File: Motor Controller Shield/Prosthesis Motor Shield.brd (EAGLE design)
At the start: 101.6 x 53.3 mm, 51 parts, among them M1_ACT M02POLAR_LOCK, M2_ACT M02POLAR_LOCK, U1 74VHC14MTCX, U2 74VHC14MTCX

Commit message: Routed BMS interface board and added branding.
Changed branding for CCB and MCBs
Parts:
- moved U$1 34.6 mm to (22.5, 11.7)
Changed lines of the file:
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@@
 <layer number="23" name="tOrigins" color="15" fill="1" visible="yes" active="yes"/>
 <layer number="24" name="bOrigins" color="15" fill="1" visible="yes" active="yes"/>
-<layer number="25" name="tNames" color="16" fill="1" visible="no" active="yes"/>
+<layer number="25" name="tNames" color="16" fill="1" visible="yes" active="yes"/>
 <layer number="26" name="bNames" color="7" fill="1" visible="no" active="yes"/>
 <layer number="27" name="tValues" color="7" fill="1" visible="no" active="yes"/>
@@
 <text x="24.13" y="22.225" size="1.27" layer="21" ratio="15" rot="R90">Motor Enable</text>
 <text x="0.635" y="34.925" size="1.27" layer="21" ratio="15" rot="SR270">Prosthesis MCB V1.0</text>
-<text x="29.21" y="12.7" size="1.27" layer="21" ratio="15" rot="SR0">Made By:
+<text x="51.1175" y="40.3225" size="1.27" layer="21" ratio="15" rot="SR0">Made By:
 Gerald Orban</text>
 </plain>
@@
 <element name="DISP" library="SparkFun-Connectors" package="MOLEX-1X4_LOCK" value="" x="43.4975" y="33.02" rot="R180"/>
 <element name="PRES_INPUT" library="SparkFun-Connectors" package="MOLEX-1X4_LOCK" value="" x="80.3275" y="19.05" rot="R270"/>
-<element name="U$1" library="prosthesis" package="PROS_LOGO" value="" x="46.0375" y="37.1475"/>
+<element name="U$1" library="prosthesis" package="PROS_LOGO" value="" x="22.5425" y="11.7475"/>
 <element name="ROCK1" library="SparkFun-Connectors" package="MOLEX-1X3_LOCK" value="" x="53.6575" y="31.75"/>
 <element name="ROCK2" library="SparkFun-Connectors" package="MOLEX-1X3_LOCK" value="" x="58.7375" y="26.3525" rot="R180"/>

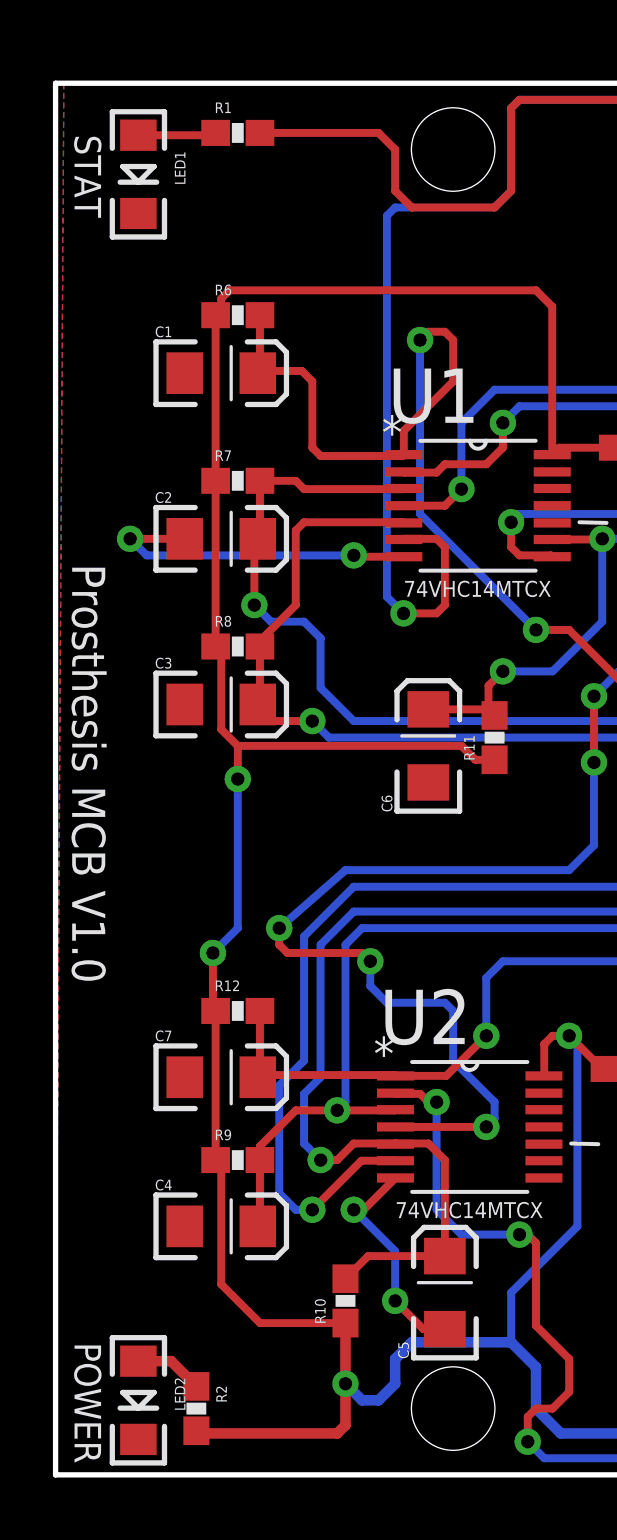
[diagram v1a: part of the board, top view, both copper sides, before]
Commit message: UPdating resistor packages to sizes which are
capable of disappating the appropriate amount of power.
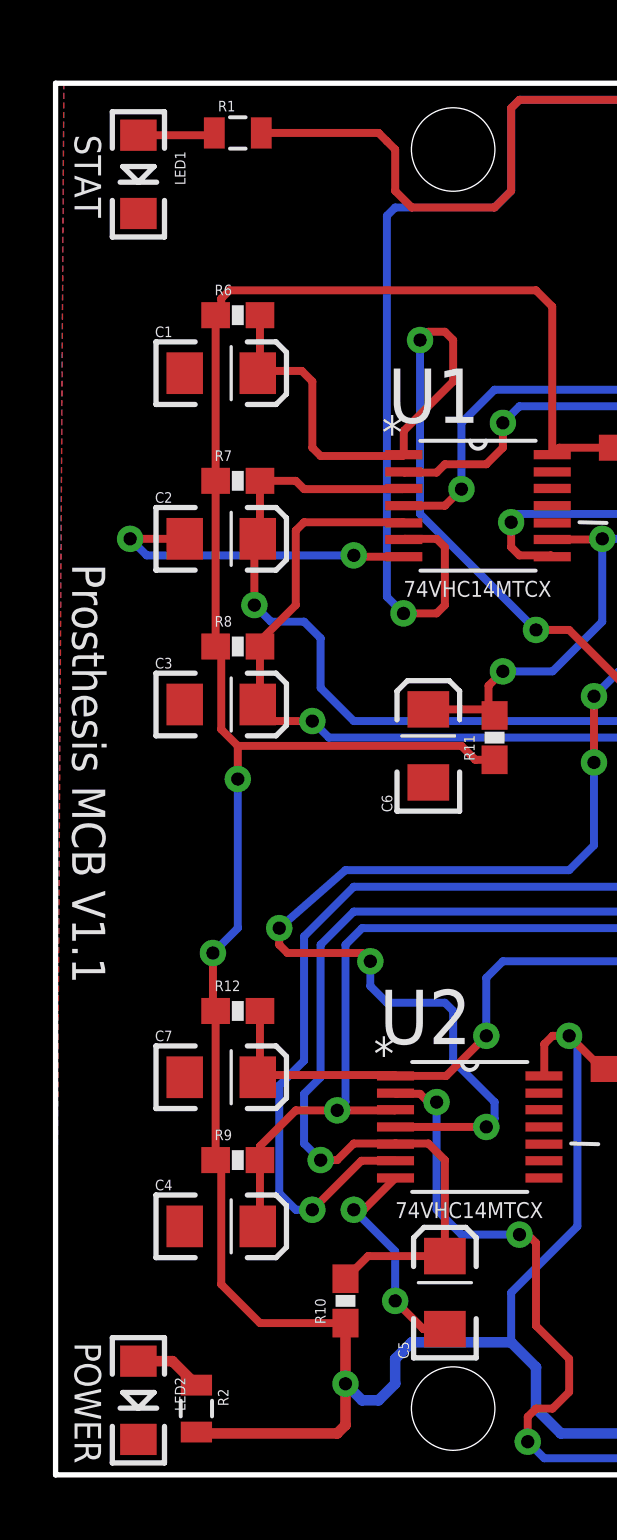
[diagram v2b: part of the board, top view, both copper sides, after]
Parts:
- R1, R2: device SparkFun-Passives:0603-RES -> SparkFun-Resistors:0805
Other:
- board text added: "Prosthesis MCB V1.1"
- board text removed: "Prosthesis MCB V1.0"
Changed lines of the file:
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@@
 <setting verticaltext="up"/>
 </settings>
-<grid distance="0.0125" unitdist="inch" unit="inch" style="lines" multiple="1" display="yes" altdistance="0.005" altunitdist="inch" altunit="inch"/>
+<grid distance="0.05" unitdist="inch" unit="inch" style="lines" multiple="1" display="yes" altdistance="0.005" altunitdist="inch" altunit="inch"/>
 <layers>
 <layer number="1" name="Top" color="4" fill="1" visible="yes" active="yes"/>
@@
 <text x="34.29" y="29.845" size="1.27" layer="21" ratio="15" rot="R90">Display</text>
 <text x="24.13" y="22.225" size="1.27" layer="21" ratio="15" rot="R90">Motor Enable</text>
-<text x="0.635" y="34.925" size="1.27" layer="21" ratio="15" rot="SR270">Prosthesis MCB V1.0</text>
+<text x="0.635" y="34.925" size="1.27" layer="21" ratio="15" rot="SR270">Prosthesis MCB V1.1</text>
 <text x="51.1175" y="40.3225" size="1.27" layer="21" ratio="15" rot="SR0">Made By:
 Gerald Orban</text>
@@
 <element name="JP12" library="SparkFun" package="1X02_LOCK" value="" x="93.98" y="50.8"/>
 <element name="PWR" library="SparkFun-Connectors" package="1X02_2.54_SCREWTERM" value="M022.54MM_SCREWTERM" x="28.575" y="3.4925" rot="R180"/>
-<element name="R1" library="SparkFun-Passives" package="0603-RES" value="330" x="6.985" y="51.435"/>
-<element name="R2" library="SparkFun-Passives" package="0603-RES" value="330" x="5.3975" y="2.54" rot="R270"/>
 <element name="LED1" library="SparkFun-LED" package="LED-1206" value="Green" x="3.175" y="49.8475" rot="R270"/>
 <element name="LED2" library="SparkFun-LED" package="LED-1206" value="Red" x="3.175" y="2.8575" rot="R270"/>
@@
 <element name="CCB1_PWR" library="SparkFun-Connectors" package="MOLEX-1X2_LOCK" value="M02POLAR_LOCK" x="85.725" y="32.0675" rot="R180"/>
 <element name="CCB2_PWR" library="SparkFun-Connectors" package="MOLEX-1X2_LOCK" value="M02POLAR_LOCK" x="83.185" y="25.7175"/>
+<element name="R2" library="SparkFun-Resistors" package="0805" value="330" x="5.3975" y="2.54" rot="R270"/>
+<element name="R1" library="SparkFun-Resistors" package="0805" value="330" x="6.985" y="51.435"/>
 </elements>
 <signals>
@@
 <signal name="5V">
 <contactref element="JP10" pad="3"/>
-<contactref element="R2" pad="2"/>
 <contactref element="U1" pad="14"/>
 <contactref element="R6" pad="1"/>
@@
 <wire x1="11.1125" y1="1.905" x2="10.795" y2="1.5875" width="0.4064" layer="1"/>
 <wire x1="10.795" y1="1.5875" x2="5.5" y2="1.5875" width="0.4064" layer="1"/>
-<wire x1="5.5" y1="1.5875" x2="5.3975" y2="1.69" width="0.4064" layer="1"/>
 <wire x1="11.1125" y1="5.8175" x2="7.835" y2="5.8175" width="0.3048" layer="1"/>
 <wire x1="7.835" y1="5.8175" x2="6.35" y2="7.3025" width="0.3048" layer="1"/>
@@
 <wire x1="6.35" y1="45.085" x2="6.35" y2="44.665" width="0.3048" layer="1"/>
 <wire x1="6.35" y1="44.665" x2="6.135" y2="44.45" width="0.3048" layer="1"/>
+<contactref element="R2" pad="2"/>
+<wire x1="5.3975" y1="1.64" x2="5.4475" y2="1.64" width="0.6096" layer="1"/>
+<wire x1="5.4475" y1="1.64" x2="5.5" y2="1.5875" width="0.6096" layer="1"/>
 </signal>
 <signal name="GND">
@@
 <signal name="D13">
 <contactref element="JP3" pad="6"/>
-<contactref element="R1" pad="2"/>
-<wire x1="7.835" y1="51.435" x2="12.3825" y2="51.435" width="0.3048" layer="1"/>
-<wire x1="12.3825" y1="51.435" x2="13.0175" y2="50.8" width="0.3048" layer="1"/>
+<wire x1="12.7" y1="51.1175" x2="13.0175" y2="50.8" width="0.3048" layer="1"/>
 <wire x1="13.0175" y1="50.8" x2="13.0175" y2="49.2125" width="0.3048" layer="1"/>
 <wire x1="13.0175" y1="49.2125" x2="13.6525" y2="48.5775" width="0.3048" layer="1"/>
@@
 <wire x1="28.8925" y1="52.705" x2="29.21" y2="52.3875" width="0.3048" layer="1"/>
 <wire x1="29.21" y1="52.3875" x2="29.21" y2="50.927" width="0.3048" layer="1"/>
+<contactref element="R1" pad="2"/>
+<wire x1="7.885" y1="51.435" x2="12.3825" y2="51.435" width="0.3048" layer="1"/>
+<wire x1="12.3825" y1="51.435" x2="12.7" y2="51.1175" width="0.3048" layer="1"/>
 </signal>
 <signal name="AREF">
@@
 </signal>
 <signal name="N$126">
+<contactref element="LED2" pad="A"/>
+<wire x1="3.175" y1="4.3575" x2="4.48" y2="4.3575" width="0.4064" layer="1"/>
 <contactref element="R2" pad="1"/>
-<contactref element="LED2" pad="A"/>
-<wire x1="3.175" y1="4.3575" x2="4.43" y2="4.3575" width="0.4064" layer="1"/>
-<wire x1="4.43" y1="4.3575" x2="5.3975" y2="3.39" width="0.4064" layer="1"/>
+<wire x1="4.48" y1="4.3575" x2="5.3975" y2="3.44" width="0.4064" layer="1"/>
 </signal>
 <signal name="N$127">
+<contactref element="LED1" pad="A"/>
 <contactref element="R1" pad="1"/>
-<contactref element="LED1" pad="A"/>
-<wire x1="3.175" y1="51.3475" x2="6.0475" y2="51.3475" width="0.3048" layer="1"/>
-<wire x1="6.0475" y1="51.3475" x2="6.135" y2="51.435" width="0.3048" layer="1"/>
+<wire x1="3.175" y1="51.3475" x2="5.9975" y2="51.3475" width="0.3048" layer="1"/>
+<wire x1="5.9975" y1="51.3475" x2="6.085" y2="51.435" width="0.3048" layer="1"/>
 </signal>
 <signal name="CON_DET">

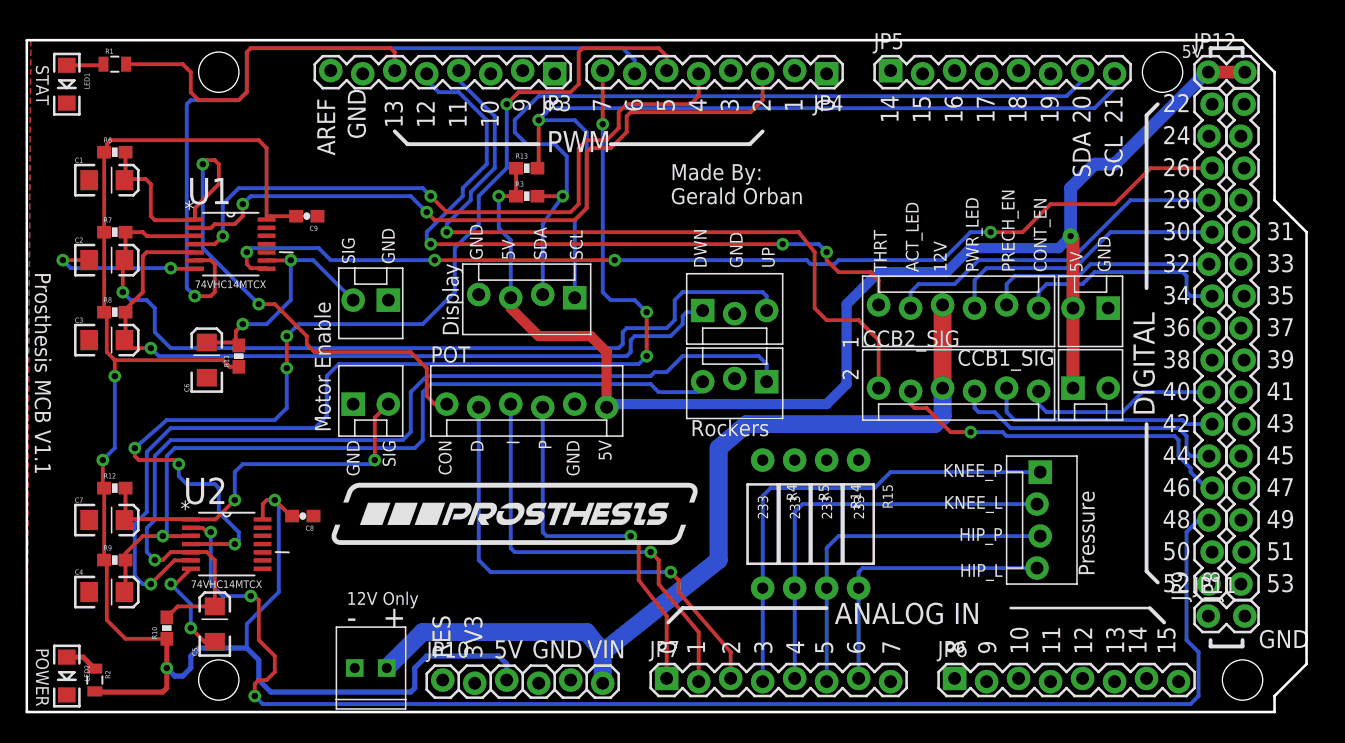
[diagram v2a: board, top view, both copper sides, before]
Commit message: Added capacitors for the three main boards
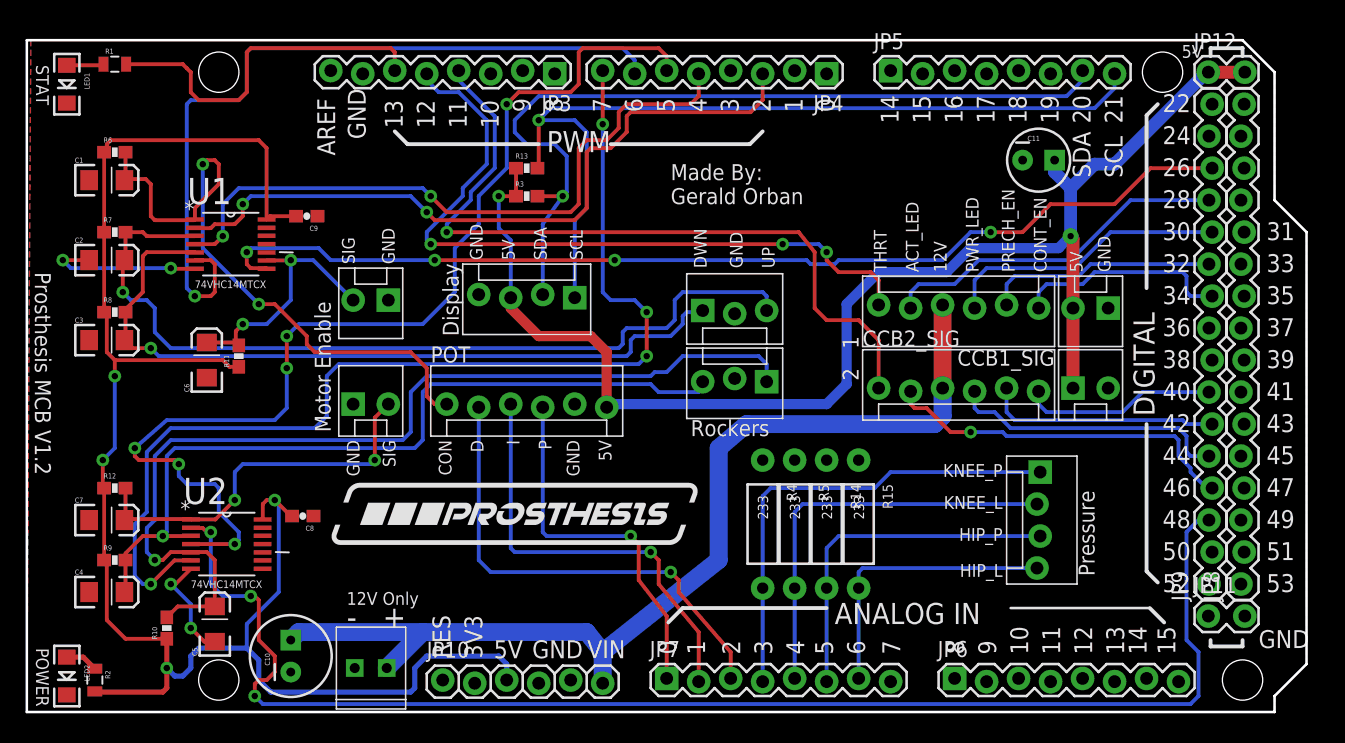
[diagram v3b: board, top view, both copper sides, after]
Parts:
- added C10: 100uF, SparkFun-Capacitors:CPOL-RADIAL-100UF-25V
- added C11: 10uF, SparkFun-Capacitors:CPOL-RADIAL-10UF-25V
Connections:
- net 5V@1: now also C11.1
- net GND: now also C10.2, C11.2
- net VIN: now also C10.1
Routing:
- net VIN: track 69.8 -> 80.5 mm
- net 5V@1: track 106.0 -> 108.8 mm
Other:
- board text added: "Prosthesis MCB V1.2"
- board text removed: "Prosthesis MCB V1.1"
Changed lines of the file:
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@@
 <text x="34.29" y="29.845" size="1.27" layer="21" ratio="15" rot="R90">Display</text>
 <text x="24.13" y="22.225" size="1.27" layer="21" ratio="15" rot="R90">Motor Enable</text>
-<text x="0.635" y="34.925" size="1.27" layer="21" ratio="15" rot="SR270">Prosthesis MCB V1.1</text>
+<text x="0.635" y="34.925" size="1.27" layer="21" ratio="15" rot="SR270">Prosthesis MCB V1.2</text>
 <text x="51.1175" y="40.3225" size="1.27" layer="21" ratio="15" rot="SR0">Made By:
 Gerald Orban</text>
@@
 <element name="R2" library="SparkFun-Resistors" package="0805" value="330" x="5.3975" y="2.54" rot="R270"/>
 <element name="R1" library="SparkFun-Resistors" package="0805" value="330" x="6.985" y="51.435"/>
+<element name="C10" library="SparkFun-Capacitors" package="CPOL-RADIAL-100UF-25V" value="100uF" x="20.955" y="4.445" rot="R90"/>
+<element name="C11" library="SparkFun-Capacitors" package="CPOL-RADIAL-10UF-25V" value="10uF" x="80.3275" y="43.815"/>
 </elements>
 <signals>
@@
 <contactref element="CCB1_PWR" pad="1"/>
 <contactref element="CCB2_PWR" pad="2"/>
+<contactref element="C10" pad="2"/>
+<contactref element="C11" pad="2"/>
 </signal>
 <signal name="VIN">
@@
 <wire x1="72.7075" y1="23.495" x2="72.7075" y2="25.7175" width="1.4224" layer="16"/>
 <wire x1="72.7075" y1="32.3215" x2="72.7075" y2="25.7175" width="1.4224" layer="1"/>
+<contactref element="C10" pad="1"/>
+<wire x1="31.4325" y1="6.35" x2="21.59" y2="6.35" width="1.4224" layer="16"/>
+<wire x1="21.59" y1="6.35" x2="20.955" y2="5.715" width="1.4224" layer="16"/>
 </signal>
 <signal name="A0">
@@
 <wire x1="83.058" y1="37.592" x2="82.8675" y2="37.7825" width="1.016" layer="1"/>
 <wire x1="83.058" y1="32.0675" x2="83.058" y2="25.7175" width="1.016" layer="1"/>
+<contactref element="C11" pad="1"/>
+<wire x1="81.5975" y1="43.815" x2="81.5975" y2="42.8625" width="1.016" layer="16"/>
+<wire x1="81.5975" y1="42.8625" x2="82.8675" y2="41.5925" width="1.016" layer="16"/>
 </signal>
 <signal name="D22">
